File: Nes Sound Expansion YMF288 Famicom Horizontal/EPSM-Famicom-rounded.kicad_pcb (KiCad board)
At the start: 2 copper layers, 99 x 91.7 mm, 68 parts, among them J1 CARTRIDGE_F, J2 CONSOLE_M, J3 AudioJack4_SwitchTR1, U1 74HC688, U10 74HC132, U11 74HC257, U12 74HC257, U13 LM358, U14 74LVC1G373, U15 74HC257, U2 74HC139, U3 74HC174, U4 74HC174, U5 74HC688, U6 74HC688, U7 74HC132, U8 YMF288, U9 BU9480F, X1 SG-8002CA

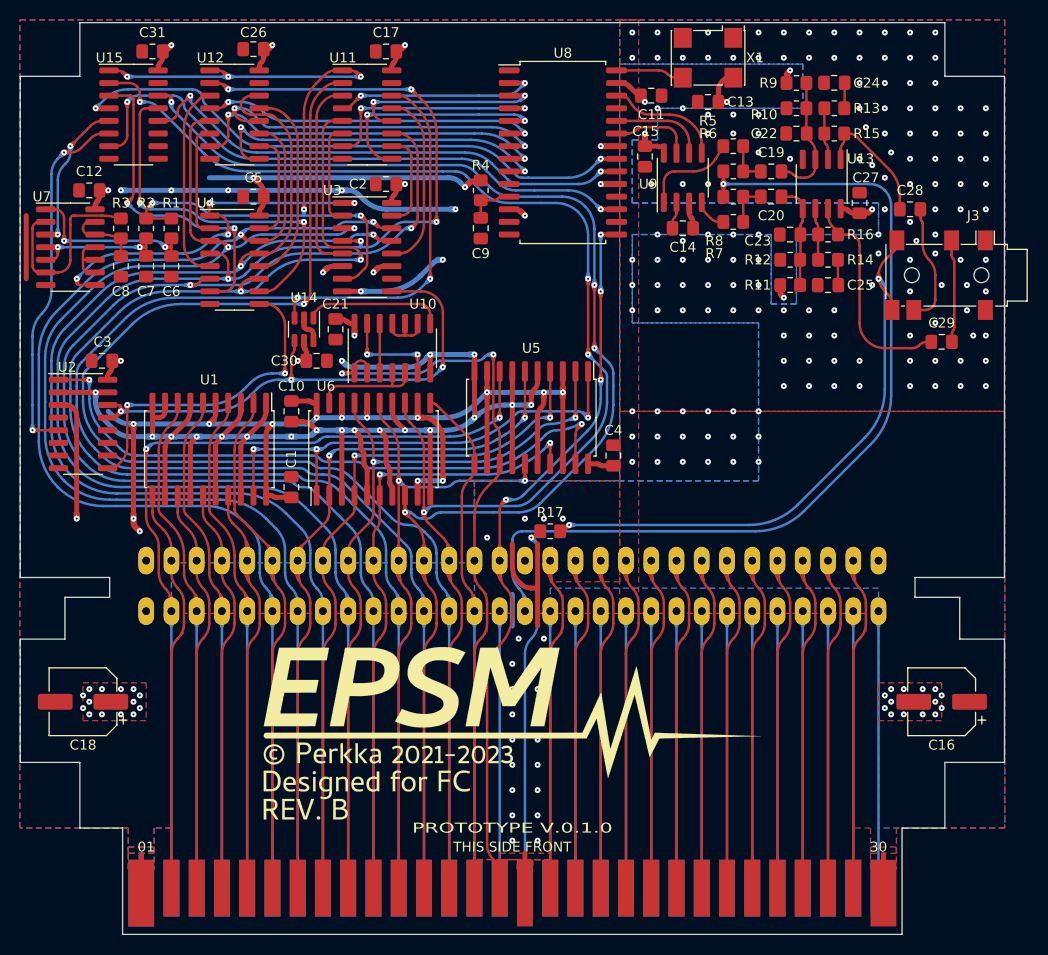
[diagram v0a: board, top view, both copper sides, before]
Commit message: Fix swapped connections
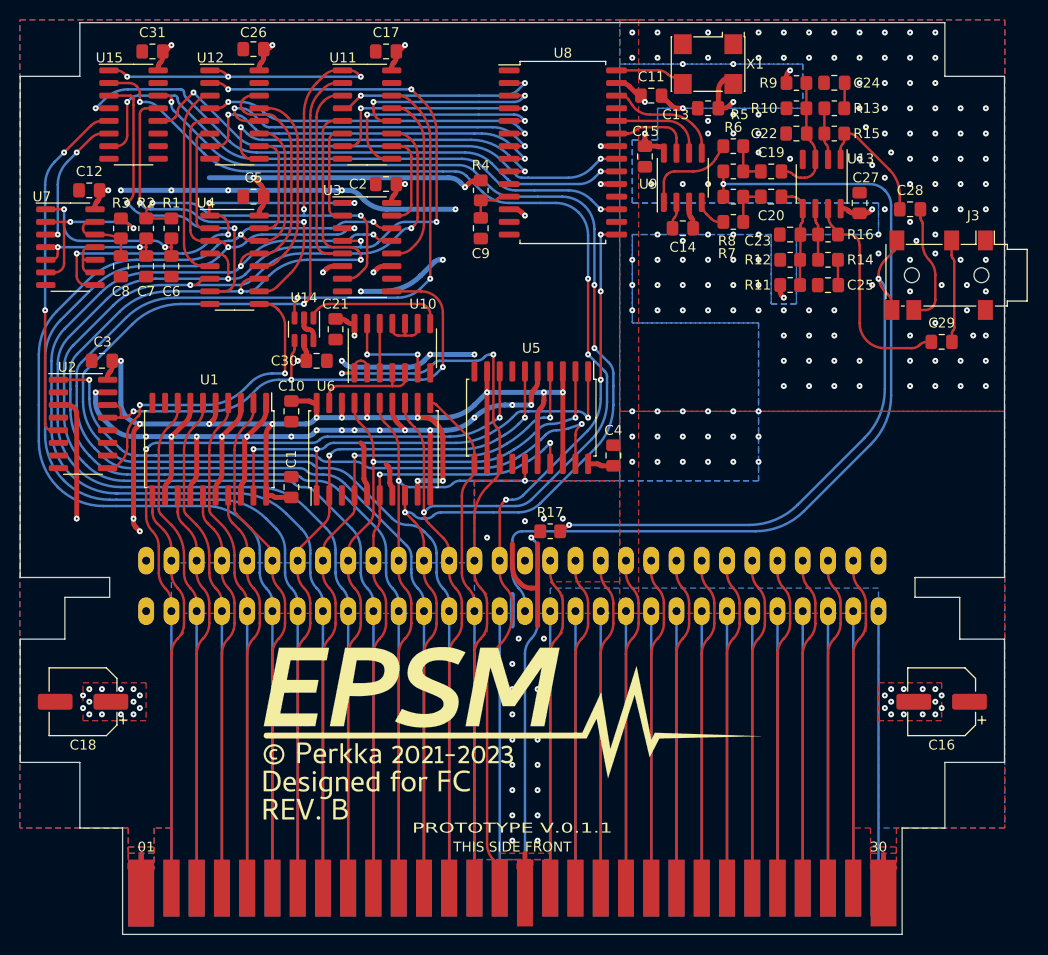
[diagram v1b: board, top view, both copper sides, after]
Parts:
- moved C13 0.63 mm to (146.7, 54.6)
- moved X1 0.63 mm to (146.7, 50.2)
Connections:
- U15 pad 12: /YM_A0 -> /YM_A1
- U15 pad 4: /YM_A1 -> /YM_A0
- U15 pad 5: /BUF_CS -> /~{CS}
- U15 pad 6: /~{CS} -> /BUF_CS
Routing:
- net GND: track 245.6 -> 197.0 mm, vias 195 -> 194
- net /YM_A1: track 58.5 -> 51.3 mm
- net /YM_A0: track 51.4 -> 58.5 mm
- net VCC: track 223.2 -> 228.2 mm
- net Net-(R3-Pad1): track 19.7 -> 17.1 mm, vias 0 -> 2
- net /FF_RESET: track 39.3 -> 40.7 mm
- net /~{CS}: track 36.6 -> 35.3 mm
- net /BUF_CS: track 15.3 -> 14.0 mm
- net /~{OUT_1}: track 32.9 -> 32.0 mm
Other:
- board text added: "PROTOTYPE V.0.1.1"
- board text removed: "PROTOTYPE V.0.1.0"
